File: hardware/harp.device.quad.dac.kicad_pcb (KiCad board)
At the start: 2 copper layers, 0 parts

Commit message: The footprint assigning and reviewing have started.
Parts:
- added C1: 100nF, Capacitor_SMD:C_0402_1005Metric, F.Cu at (122.2, 49.0)
- added C10: 10uF, Capacitor_SMD:C_0805_2012Metric, F.Cu at (118.5, 49.5)
- added C100: 100nF, Capacitor_SMD:C_0402_1005Metric, F.Cu at (77.7, 74.6)
- added C101: 100nF, Capacitor_SMD:C_0402_1005Metric, F.Cu at (77.7, 76.6)
- added C102: 100nF, Capacitor_SMD:C_0402_1005Metric, F.Cu at (80.5, 70.7)
- added C103: 100nF, Capacitor_SMD:C_0402_1005Metric, F.Cu at (80.5, 72.7)
- added C104: 100nF, Capacitor_SMD:C_0402_1005Metric, F.Cu at (80.5, 74.6)
- added C105: 100nF, Capacitor_SMD:C_0402_1005Metric, F.Cu at (80.5, 76.6)
- added C106: 10uF, Capacitor_SMD:C_0805_2012Metric, F.Cu at (96.7, 66.6)
- added C107: 100nF, Capacitor_SMD:C_0402_1005Metric, F.Cu at (83.4, 70.7)
- added C108: 1uF, Capacitor_SMD:C_0402_1005Metric, F.Cu at (83.4, 72.7)
- added C109: 10uF, Capacitor_SMD:C_0805_2012Metric, F.Cu at (96.7, 69.6)
- added C11: 10uF, Capacitor_SMD:C_0805_2012Metric, F.Cu at (118.5, 52.6)
- added C110: 100nF, Capacitor_SMD:C_0402_1005Metric, F.Cu at (83.4, 74.6)
- added C111: 1uF, Capacitor_SMD:C_0402_1005Metric, F.Cu at (83.4, 76.6)
- added C112: 10uF, Capacitor_SMD:C_0805_2012Metric, F.Cu at (96.7, 72.6)
- added C113: 100nF, Capacitor_SMD:C_0402_1005Metric, F.Cu at (96.2, 95.6)
- added C114: 100nF, Capacitor_SMD:C_0402_1005Metric, F.Cu at (96.2, 97.6)
- added C115: 100nF, Capacitor_SMD:C_0402_1005Metric, F.Cu at (96.2, 99.5)
- added C116: 100nF, Capacitor_SMD:C_0402_1005Metric, F.Cu at (96.2, 101.5)
- added C117: 100nF, Capacitor_SMD:C_0402_1005Metric, F.Cu at (96.2, 103.5)
- added C118: 1uF, Capacitor_SMD:C_0402_1005Metric, F.Cu at (96.2, 105.5)
- added C119: 10uF, Capacitor_SMD:C_0805_2012Metric, F.Cu at (88.3, 81.1)
- added C12: 100nF, Capacitor_SMD:C_0402_1005Metric, F.Cu at (125.0, 53.0)
- added C120: 10uF, Capacitor_SMD:C_0805_2012Metric, F.Cu at (88.3, 84.1)
- added C121: 100nF, Capacitor_SMD:C_0402_1005Metric, F.Cu at (96.2, 107.4)
- added C122: 4.7uF, Capacitor_SMD:C_0805_2012Metric, F.Cu at (88.3, 87.1)
- added C123: 1uF, Capacitor_SMD:C_0402_1005Metric, F.Cu at (99.1, 95.6)
- added C124: 1uF, Capacitor_SMD:C_0402_1005Metric, F.Cu at (99.1, 97.6)
- added C125: 10uF, Capacitor_SMD:C_0805_2012Metric, F.Cu at (88.3, 90.1)
- added C126: 10uF, Capacitor_SMD:C_0805_2012Metric, F.Cu at (88.3, 93.1)
- added C127: 10uF, Capacitor_SMD:C_0805_2012Metric, F.Cu at (92.8, 81.1)
- added C128: 10uF, Capacitor_SMD:C_0805_2012Metric, F.Cu at (92.8, 84.1)
- added C129: 150pF, Capacitor_SMD:C_0402_1005Metric, F.Cu at (99.1, 99.5)
- added C13: 100nF, Capacitor_SMD:C_0402_1005Metric, F.Cu at (125.0, 54.9)
- added C130: 100nF, Capacitor_SMD:C_0402_1005Metric, F.Cu at (99.1, 101.5)
- added C131: 330pF, Capacitor_SMD:C_0402_1005Metric, F.Cu at (99.1, 103.5)
- added C132: 10pF, Capacitor_SMD:C_0402_1005Metric, F.Cu at (99.1, 105.5)
- added C133: 33nF, Capacitor_SMD:C_0402_1005Metric, F.Cu at (99.1, 107.4)
- added C134: 1nF, Capacitor_SMD:C_0402_1005Metric, F.Cu at (102.0, 95.6)
- added C135: 100nF, Capacitor_SMD:C_0402_1005Metric, F.Cu at (102.0, 97.6)
- added C136: 100nF, Capacitor_SMD:C_0402_1005Metric, F.Cu at (102.0, 99.5)
- added C137: 1uF, Capacitor_SMD:C_0402_1005Metric, F.Cu at (102.0, 101.5)
- added C138: 1uF, Capacitor_SMD:C_0402_1005Metric, F.Cu at (102.0, 103.5)
- added C139: 10uF, Capacitor_SMD:C_0805_2012Metric, F.Cu at (92.8, 87.1)
- added C14: 100nF, Capacitor_SMD:C_0402_1005Metric, F.Cu at (125.0, 56.9)
- added C140: 10uF, Capacitor_SMD:C_0805_2012Metric, F.Cu at (92.8, 90.1)
- added C141: 10uF, Capacitor_SMD:C_0805_2012Metric, F.Cu at (92.8, 93.1)
- added C142: 10uF, Capacitor_SMD:C_0805_2012Metric, F.Cu at (97.2, 81.1)
- added C143: 10uF, Capacitor_SMD:C_0805_2012Metric, F.Cu at (97.2, 84.1)
- added C144: 10uF, Capacitor_SMD:C_0805_2012Metric, F.Cu at (97.2, 87.1)
- added C145: 4.7uF, Capacitor_SMD:C_0805_2012Metric, F.Cu at (97.2, 90.1)
- added C146: 100nF, Capacitor_SMD:C_0402_1005Metric, F.Cu at (102.0, 105.5)
- added C147: 100nF, Capacitor_SMD:C_0402_1005Metric, F.Cu at (102.0, 107.4)
- added C148: 100nF, Capacitor_SMD:C_0402_1005Metric, F.Cu at (139.8, 101.8)
- added C149: 100nF, Capacitor_SMD:C_0402_1005Metric, F.Cu at (139.8, 103.7)
- added C15: 100nF, Capacitor_SMD:C_0402_1005Metric, F.Cu at (125.0, 58.9)
- added C150: 100nF, Capacitor_SMD:C_0402_1005Metric, F.Cu at (139.8, 105.7)
- added C151: 100nF, Capacitor_SMD:C_0402_1005Metric, F.Cu at (139.8, 107.7)
- added C16: 4.7uF, Capacitor_SMD:C_0805_2012Metric, F.Cu at (118.5, 55.6)
- added C17: 4.7uF, Capacitor_SMD:C_0805_2012Metric, F.Cu at (118.5, 58.6)
- added C18: 10uF, Capacitor_SMD:C_0805_2012Metric, F.Cu at (118.5, 61.6)
- added C19: 100nF, Capacitor_SMD:C_0402_1005Metric, F.Cu at (125.0, 60.9)
- added C2: 100nF, Capacitor_SMD:C_0402_1005Metric, F.Cu at (122.2, 51.0)
- added C20: 100nF, Capacitor_SMD:C_0402_1005Metric, F.Cu at (127.9, 49.0)
- added C21: 100nF, Capacitor_SMD:C_0402_1005Metric, F.Cu at (127.9, 51.0)
- added C22: 100nF, Capacitor_SMD:C_0402_1005Metric, F.Cu at (127.9, 53.0)
- added C23: 100nF, Capacitor_SMD:C_0402_1005Metric, F.Cu at (127.9, 54.9)
- added C24: 100nF, Capacitor_SMD:C_0402_1005Metric, F.Cu at (127.9, 56.9)
- added C25: 100nF, Capacitor_SMD:C_0402_1005Metric, F.Cu at (127.9, 58.9)
- added C26: 100nF, Capacitor_SMD:C_0402_1005Metric, F.Cu at (127.9, 60.9)
- added C27: 100nF, Capacitor_SMD:C_0402_1005Metric, F.Cu at (130.8, 49.0)
- added C28: 100nF, Capacitor_SMD:C_0402_1005Metric, F.Cu at (130.8, 51.0)
- added C29: 100nF, Capacitor_SMD:C_0402_1005Metric, F.Cu at (130.8, 53.0)
- added C3: 1nF, Capacitor_SMD:C_0402_1005Metric, F.Cu at (122.2, 53.0)
- added C30: 100nF, Capacitor_SMD:C_0402_1005Metric, F.Cu at (144.4, 49.0)
- added C31: 1uF, Capacitor_SMD:C_0402_1005Metric, F.Cu at (144.4, 51.0)
- added C32: 100nF, Capacitor_SMD:C_0402_1005Metric, F.Cu at (144.4, 53.0)
- added C33: 100nF, Capacitor_SMD:C_0402_1005Metric, F.Cu at (144.4, 54.9)
- added C34: 100nF, Capacitor_SMD:C_0402_1005Metric, F.Cu at (144.4, 56.9)
- added C35: 100nF, Capacitor_SMD:C_0402_1005Metric, F.Cu at (144.4, 58.9)
- added C36: 10uF, Capacitor_SMD:C_0805_2012Metric, F.Cu at (149.6, 63.3)
- added C37: 100nF, Capacitor_SMD:C_0402_1005Metric, F.Cu at (144.4, 60.9)
- added C38: 1uF, Capacitor_SMD:C_0402_1005Metric, F.Cu at (147.2, 49.0)
- added C39: 100nF, Capacitor_SMD:C_0402_1005Metric, F.Cu at (147.2, 51.0)
- added C4: 100nF, Capacitor_SMD:C_0402_1005Metric, F.Cu at (122.2, 54.9)
- added C40: 100nF, Capacitor_SMD:C_0402_1005Metric, F.Cu at (147.2, 53.0)
- added C41: 100nF, Capacitor_SMD:C_0402_1005Metric, F.Cu at (147.2, 54.9)
- added C42: 100nF, Capacitor_SMD:C_0402_1005Metric, F.Cu at (147.2, 56.9)
- added C43: 1uF, Capacitor_SMD:C_0402_1005Metric, F.Cu at (147.2, 58.9)
- added C44: 100nF, Capacitor_SMD:C_0402_1005Metric, F.Cu at (147.2, 60.9)
- added C45: 100nF, Capacitor_SMD:C_0402_1005Metric, F.Cu at (150.1, 49.0)
- added C46: 100nF, Capacitor_SMD:C_0402_1005Metric, F.Cu at (150.1, 51.0)
- added C47: 100nF, Capacitor_SMD:C_0402_1005Metric, F.Cu at (150.1, 53.0)
- added C48: 1uF, Capacitor_SMD:C_0402_1005Metric, F.Cu at (150.1, 54.9)
- added C49: 100nF, Capacitor_SMD:C_0402_1005Metric, F.Cu at (150.1, 56.9)
- added C5: 100nF, Capacitor_SMD:C_0402_1005Metric, F.Cu at (122.2, 56.9)
- added C50: 15pF, Capacitor_SMD:C_0402_1005Metric, F.Cu at (150.1, 58.9)
- added C51: 15pF, Capacitor_SMD:C_0402_1005Metric, F.Cu at (150.1, 60.9)
- added C52: 15pF, Capacitor_SMD:C_0402_1005Metric, F.Cu at (153.0, 49.0)
- added C53: 15pF, Capacitor_SMD:C_0402_1005Metric, F.Cu at (153.0, 51.0)
- added C54: 15pF, Capacitor_SMD:C_0402_1005Metric, F.Cu at (153.0, 53.0)
- added C55: 15pF, Capacitor_SMD:C_0402_1005Metric, F.Cu at (153.0, 54.9)
- added C56: 15pF, Capacitor_SMD:C_0402_1005Metric, F.Cu at (153.0, 56.9)
- added C57: 15pF, Capacitor_SMD:C_0402_1005Metric, F.Cu at (153.0, 58.9)
- added C58: 10uF, Capacitor_SMD:C_0805_2012Metric, F.Cu at (149.6, 66.3)
- added C59: 10uF, Capacitor_SMD:C_0805_2012Metric, F.Cu at (149.6, 69.4)
- added C6: 10nF, Capacitor_SMD:C_0402_1005Metric, F.Cu at (122.2, 58.9)
- added C60: 15pF, Capacitor_SMD:C_0402_1005Metric, F.Cu at (121.9, 76.8)
- added C61: 15pF, Capacitor_SMD:C_0402_1005Metric, F.Cu at (121.9, 78.7)
- added C62: 15pF, Capacitor_SMD:C_0402_1005Metric, F.Cu at (121.9, 80.7)
- added C63: 15pF, Capacitor_SMD:C_0402_1005Metric, F.Cu at (121.9, 82.7)
- added C64: 100nF, Capacitor_SMD:C_0402_1005Metric, F.Cu at (121.9, 84.6)
- added C65: 100nF, Capacitor_SMD:C_0402_1005Metric, F.Cu at (121.9, 86.6)
- added C66: 100nF, Capacitor_SMD:C_0402_1005Metric, F.Cu at (121.9, 88.6)
- added C67: 100nF, Capacitor_SMD:C_0402_1005Metric, F.Cu at (121.9, 90.5)
- added C68: 100nF, Capacitor_SMD:C_0402_1005Metric, F.Cu at (124.8, 76.8)
- added C69: 100nF, Capacitor_SMD:C_0402_1005Metric, F.Cu at (124.8, 78.7)
- added C7: 1uF, Capacitor_SMD:C_0402_1005Metric, F.Cu at (122.2, 60.9)
- added C70: 100nF, Capacitor_SMD:C_0402_1005Metric, F.Cu at (124.8, 80.7)
- added C71: 100nF, Capacitor_SMD:C_0402_1005Metric, F.Cu at (124.8, 82.7)
- added C72: 100nF, Capacitor_SMD:C_0402_1005Metric, F.Cu at (124.8, 84.6)
- added C73: 100nF, Capacitor_SMD:C_0402_1005Metric, F.Cu at (124.8, 86.6)
- added C74: 100nF, Capacitor_SMD:C_0402_1005Metric, F.Cu at (124.8, 88.6)
- added C75: 100nF, Capacitor_SMD:C_0402_1005Metric, F.Cu at (124.8, 90.5)
- added C76: 100nF, Capacitor_SMD:C_0402_1005Metric, F.Cu at (127.7, 76.8)
- added C77: 100nF, Capacitor_SMD:C_0402_1005Metric, F.Cu at (127.7, 78.7)
- added C78: 100nF, Capacitor_SMD:C_0402_1005Metric, F.Cu at (127.7, 80.7)
- added C79: 100nF, Capacitor_SMD:C_0402_1005Metric, F.Cu at (127.7, 82.7)
- added C8: 1uF, Capacitor_SMD:C_0402_1005Metric, F.Cu at (125.0, 49.0)
- added C80: 15pF, Capacitor_SMD:C_0402_1005Metric, F.Cu at (127.7, 84.6)
- added C81: 15pF, Capacitor_SMD:C_0402_1005Metric, F.Cu at (127.7, 86.6)
- added C82: 15pF, Capacitor_SMD:C_0402_1005Metric, F.Cu at (127.7, 88.6)
- added C83: 15pF, Capacitor_SMD:C_0402_1005Metric, F.Cu at (127.7, 90.5)
- added C84: 100nF, Capacitor_SMD:C_0402_1005Metric, F.Cu at (130.5, 76.8)
- added C85: 100nF, Capacitor_SMD:C_0402_1005Metric, F.Cu at (130.5, 78.7)
- added C86: 100nF, Capacitor_SMD:C_0402_1005Metric, F.Cu at (130.5, 80.7)
- added C87: 100nF, Capacitor_SMD:C_0402_1005Metric, F.Cu at (130.5, 82.7)
- added C88: 100nF, Capacitor_SMD:C_0402_1005Metric, F.Cu at (130.5, 84.6)
- added C89: 100nF, Capacitor_SMD:C_0402_1005Metric, F.Cu at (130.5, 86.6)
- added C9: 100nF, Capacitor_SMD:C_0402_1005Metric, F.Cu at (125.0, 51.0)
- added C90: 100nF, Capacitor_SMD:C_0402_1005Metric, F.Cu at (130.5, 88.6)
- added C91: 100nF, Capacitor_SMD:C_0402_1005Metric, F.Cu at (130.5, 90.5)
- added C92: 100nF, Capacitor_SMD:C_0402_1005Metric, F.Cu at (148.3, 76.8)
- added C93: 100nF, Capacitor_SMD:C_0402_1005Metric, F.Cu at (148.3, 78.7)
- added C94: 100nF, Capacitor_SMD:C_0402_1005Metric, F.Cu at (148.3, 80.7)
- added C95: 1uF, Capacitor_SMD:C_0402_1005Metric, F.Cu at (148.3, 82.7)
- added C96: 1uF, Capacitor_SMD:C_0402_1005Metric, F.Cu at (148.3, 84.6)
- added C97: 100nF, Capacitor_SMD:C_0402_1005Metric, F.Cu at (148.3, 86.6)
- added C98: 1uF, Capacitor_SMD:C_0402_1005Metric, F.Cu at (77.7, 70.7)
- added C99: 100nF, Capacitor_SMD:C_0402_1005Metric, F.Cu at (77.7, 72.7)
- added D1: BAT43W-V, Diode_SMD:D_SOD-123, F.Cu at (123.4, 93.2)
- added D2: BAT43W-V, Diode_SMD:D_SOD-123, F.Cu at (123.4, 96.6)
- added D3: BAT43W-V, Diode_SMD:D_SOD-123, F.Cu at (123.4, 99.9)
- added D4: BAT43W-V, Diode_SMD:D_SOD-123, F.Cu at (123.4, 103.3)
- added D7: BZV55B15, Diode_SMD:D_MiniMELF, F.Cu at (79.4, 97.9)
- added D8: BZV55B15, Diode_SMD:D_MiniMELF, F.Cu at (79.4, 101.2)
- added FID1: Fiducial, Fiducial:Fiducial_0.5mm_Mask1mm, F.Cu at (130.7, 63.1)
- added FID2: Fiducial, Fiducial:Fiducial_0.5mm_Mask1mm, F.Cu at (130.7, 65.7)
- added FID3: Fiducial, Fiducial:Fiducial_0.5mm_Mask1mm, F.Cu at (130.7, 68.2)
- added FID4: Fiducial, Fiducial:Fiducial_0.5mm_Mask1mm, F.Cu at (130.7, 70.8)
- added J2: Conn_01x03_Male, Connector_PinHeader_2.54mm:PinHeader_1x03_P2.54mm_Vertical, F.Cu at (152.1, 78.1)
- added J3: USB_C_Receptacle_USB2.0, Connector_USB:USB_C_Receptacle_JAE_DX07S016JA1R1500, F.Cu at (140.0, 92.6)
- added J4: AudioJack3, Connector_Audio:Jack_3.5mm_CUI_SJ-3524-SMT_Horizontal, F.Cu at (82.3, 57.6)
- added J9: Barrel_Jack_Switch, Connector_BarrelJack:BarrelJack_CUI_PJ-102AH_Horizontal, F.Cu at (94.0, 50.4)
- added LED1: LED, LED_SMD:LED_0603_1608Metric_Pad1.05x0.95mm_HandSolder, F.Cu at (118.5, 64.4)
- added LED2: LED, LED_SMD:LED_0603_1608Metric_Pad1.05x0.95mm_HandSolder, F.Cu at (118.5, 67.0)
- added LED3: LED, LED_SMD:LED_0603_1608Metric_Pad1.05x0.95mm_HandSolder, F.Cu at (118.5, 69.6)
- added LED4: LED, LED_SMD:LED_0603_1608Metric_Pad1.05x0.95mm_HandSolder, F.Cu at (145.2, 63.1)
- added LED5: LED, LED_SMD:LED_0603_1608Metric_Pad1.05x0.95mm_HandSolder, F.Cu at (145.2, 65.7)
- added LED6: LED, LED_SMD:LED_0603_1608Metric_Pad1.05x0.95mm_HandSolder, F.Cu at (145.2, 68.3)
- added LED7: LED, LED_SMD:LED_0603_1608Metric_Pad1.05x0.95mm_HandSolder, F.Cu at (145.2, 70.9)
- added LED8: LED, LED_SMD:LED_0603_1608Metric_Pad1.05x0.95mm_HandSolder, F.Cu at (155.1, 95.0)
- added LED9: LED, LED_SMD:LED_0603_1608Metric_Pad1.05x0.95mm_HandSolder, F.Cu at (78.4, 104.2)
- added R1: 100, Resistor_SMD:R_0402_1005Metric, F.Cu at (122.2, 62.8)
- added R10: 201, Resistor_SMD:R_0402_1005Metric, F.Cu at (125.1, 68.8)
- added R100: 1.10k, Resistor_SMD:R_0402_1005Metric, F.Cu at (87.5, 97.6)
- added R101: 4.27k, Resistor_SMD:R_0402_1005Metric, F.Cu at (87.5, 99.6)
- added R102: 1.42k, Resistor_SMD:R_0402_1005Metric, F.Cu at (87.5, 101.6)
- added R103: 1.82k, Resistor_SMD:R_0402_1005Metric, F.Cu at (87.5, 103.6)
- added R104: 2.74k, Resistor_SMD:R_0402_1005Metric, F.Cu at (87.5, 105.6)
- added R105: 1.18k, Resistor_SMD:R_0402_1005Metric, F.Cu at (87.5, 107.6)
- added R106: 11.8k, Resistor_SMD:R_0402_1005Metric, F.Cu at (90.4, 95.6)
- added R107: 470, Resistor_SMD:R_0402_1005Metric, F.Cu at (90.4, 97.6)
- added R108: 57.6k, Resistor_SMD:R_0402_1005Metric, F.Cu at (90.4, 99.6)
- added R109: 365k, Resistor_SMD:R_0402_1005Metric, F.Cu at (90.4, 101.6)
- added R11: 201, Resistor_SMD:R_0402_1005Metric, F.Cu at (125.1, 70.8)
- added R110: 1.5k, Resistor_SMD:R_0402_1005Metric, F.Cu at (90.4, 103.6)
- added R111: 130k, Resistor_SMD:R_0402_1005Metric, F.Cu at (90.4, 105.6)
- added R112: 11.3k, Resistor_SMD:R_0402_1005Metric, F.Cu at (90.4, 107.6)
- added R113: 100k, Resistor_SMD:R_0402_1005Metric, F.Cu at (93.3, 95.6)
- added R114: 24.9k, Resistor_SMD:R_0402_1005Metric, F.Cu at (93.3, 97.6)
- added R115: 100k, Resistor_SMD:R_0402_1005Metric, F.Cu at (93.3, 99.6)
- added R116: 13.7k, Resistor_SMD:R_0402_1005Metric, F.Cu at (93.3, 101.6)
- added R117: 80.6k, Resistor_SMD:R_0402_1005Metric, F.Cu at (93.3, 103.6)
- added R118: 0, Resistor_SMD:R_0402_1005Metric, F.Cu at (93.3, 105.6)
- added R119: 0, Resistor_SMD:R_0402_1005Metric, F.Cu at (93.3, 107.6)
- added R12: 330, Resistor_SMD:R_0402_1005Metric, F.Cu at (125.1, 72.8)
- added R120: 10, Resistor_SMD:R_0603_1608Metric_Pad0.98x0.95mm_HandSolder, F.Cu at (136.1, 102.0)
- added R121: 10, Resistor_SMD:R_0603_1608Metric_Pad0.98x0.95mm_HandSolder, F.Cu at (136.1, 104.5)
- added R122: 10, Resistor_SMD:R_0603_1608Metric_Pad0.98x0.95mm_HandSolder, F.Cu at (136.1, 107.1)
- added R123: 10, Resistor_SMD:R_0603_1608Metric_Pad0.98x0.95mm_HandSolder, F.Cu at (136.1, 109.6)
- added R13: 330, Resistor_SMD:R_0402_1005Metric, F.Cu at (128.0, 62.8)
- added R14: 330, Resistor_SMD:R_0402_1005Metric, F.Cu at (128.0, 64.8)
- added R15: 10K, Resistor_SMD:R_0402_1005Metric, F.Cu at (128.0, 66.8)
- added R16: 10K, Resistor_SMD:R_0402_1005Metric, F.Cu at (128.0, 68.8)
- added R17: 10K, Resistor_SMD:R_0402_1005Metric, F.Cu at (128.0, 70.8)
- added R18: 330, Resistor_SMD:R_0402_1005Metric, F.Cu at (135.7, 49.0)
- added R19: 330, Resistor_SMD:R_0402_1005Metric, F.Cu at (135.7, 51.0)
- added R2: 1K, Resistor_SMD:R_0402_1005Metric, F.Cu at (122.2, 64.8)
- added R20: 330, Resistor_SMD:R_0402_1005Metric, F.Cu at (135.7, 53.0)
- added R21: 330, Resistor_SMD:R_0402_1005Metric, F.Cu at (135.7, 55.0)
- added R22: 100, Resistor_SMD:R_0402_1005Metric, F.Cu at (135.7, 57.0)
- added R23: 40.2k, Resistor_SMD:R_0402_1005Metric, F.Cu at (135.7, 59.0)
- added R24: 40.2k, Resistor_SMD:R_0402_1005Metric, F.Cu at (135.7, 61.0)
- added R25: 40.2k, Resistor_SMD:R_0402_1005Metric, F.Cu at (138.6, 49.0)
- added R26: 40.2k, Resistor_SMD:R_0402_1005Metric, F.Cu at (138.6, 51.0)
- added R27: 40.2k, Resistor_SMD:R_0402_1005Metric, F.Cu at (138.6, 53.0)
- added R28: 40.2k, Resistor_SMD:R_0402_1005Metric, F.Cu at (138.6, 55.0)
- added R29: 40.2k, Resistor_SMD:R_0402_1005Metric, F.Cu at (138.6, 57.0)
- added R3: 10, Resistor_SMD:R_0402_1005Metric, F.Cu at (122.2, 66.8)
- added R30: 40.2k, Resistor_SMD:R_0402_1005Metric, F.Cu at (138.6, 59.0)
- added R31: 10k, Resistor_SMD:R_0402_1005Metric, F.Cu at (138.6, 61.0)
- added R32: 10k, Resistor_SMD:R_0402_1005Metric, F.Cu at (141.5, 49.0)
- added R33: 10k, Resistor_SMD:R_0402_1005Metric, F.Cu at (141.5, 51.0)
- added R34: 10k, Resistor_SMD:R_0402_1005Metric, F.Cu at (141.5, 53.0)
- added R35: 10k, Resistor_SMD:R_0402_1005Metric, F.Cu at (141.5, 55.0)
- added R36: 10k, Resistor_SMD:R_0402_1005Metric, F.Cu at (141.5, 57.0)
- added R37: 10k, Resistor_SMD:R_0402_1005Metric, F.Cu at (141.5, 59.0)
- added R38: 10k, Resistor_SMD:R_0402_1005Metric, F.Cu at (141.5, 61.0)
- added R39: 4.02k, Resistor_SMD:R_0402_1005Metric, F.Cu at (107.4, 76.8)
- added R4: 10, Resistor_SMD:R_0402_1005Metric, F.Cu at (122.2, 68.8)
- added R40: 4.02k, Resistor_SMD:R_0402_1005Metric, F.Cu at (107.4, 78.8)
- added R41: 4.02k, Resistor_SMD:R_0402_1005Metric, F.Cu at (107.4, 80.8)
- added R42: 4.02k, Resistor_SMD:R_0402_1005Metric, F.Cu at (107.4, 82.7)
- added R43: 40.2k, Resistor_SMD:R_0402_1005Metric, F.Cu at (107.4, 84.7)
- added R44: 40.2k, Resistor_SMD:R_0402_1005Metric, F.Cu at (107.4, 86.7)
- added R45: 40.2k, Resistor_SMD:R_0402_1005Metric, F.Cu at (107.4, 88.7)
- added R46: 40.2k, Resistor_SMD:R_0402_1005Metric, F.Cu at (107.4, 90.7)
- added R47: 100k, Resistor_SMD:R_0402_1005Metric, F.Cu at (107.4, 92.7)
- added R48: 100k, Resistor_SMD:R_0402_1005Metric, F.Cu at (110.3, 76.8)
- added R49: 100k, Resistor_SMD:R_0402_1005Metric, F.Cu at (110.3, 78.8)
- added R5: 10, Resistor_SMD:R_0402_1005Metric, F.Cu at (122.2, 70.8)
- added R50: 100k, Resistor_SMD:R_0402_1005Metric, F.Cu at (110.3, 80.8)
- added R51: 4.75k, Resistor_SMD:R_0402_1005Metric, F.Cu at (110.3, 82.7)
- added R52: 4.75k, Resistor_SMD:R_0402_1005Metric, F.Cu at (110.3, 84.7)
- added R53: 4.75k, Resistor_SMD:R_0402_1005Metric, F.Cu at (110.3, 86.7)
- added R54: 4.75k, Resistor_SMD:R_0402_1005Metric, F.Cu at (110.3, 88.7)
- added R55: 4.75k, Resistor_SMD:R_0402_1005Metric, F.Cu at (110.3, 90.7)
- added R56: 4.75k, Resistor_SMD:R_0402_1005Metric, F.Cu at (110.3, 92.7)
- added R57: 4.75k, Resistor_SMD:R_0402_1005Metric, F.Cu at (113.2, 76.8)
- added R58: 4.75k, Resistor_SMD:R_0402_1005Metric, F.Cu at (113.2, 78.8)
- added R59: 47.5k, Resistor_SMD:R_0402_1005Metric, F.Cu at (113.2, 80.8)
- added R6: 10K, Resistor_SMD:R_0402_1005Metric, F.Cu at (122.2, 72.8)
- added R60: 10k, Resistor_SMD:R_0402_1005Metric, F.Cu at (113.2, 82.7)
- added R61: 47.5k, Resistor_SMD:R_0402_1005Metric, F.Cu at (113.2, 84.7)
- added R62: 10k, Resistor_SMD:R_0402_1005Metric, F.Cu at (113.2, 86.7)
- added R63: 47.5k, Resistor_SMD:R_0402_1005Metric, F.Cu at (113.2, 88.7)
- added R64: 10k, Resistor_SMD:R_0402_1005Metric, F.Cu at (113.2, 90.7)
- added R65: 47.5k, Resistor_SMD:R_0402_1005Metric, F.Cu at (113.2, 92.7)
- added R66: 10k, Resistor_SMD:R_0402_1005Metric, F.Cu at (116.1, 76.8)
- added R67: 40.2k, Resistor_SMD:R_0402_1005Metric, F.Cu at (116.1, 78.8)
- added R68: 40.2k, Resistor_SMD:R_0402_1005Metric, F.Cu at (116.1, 80.8)
- added R69: 40.2k, Resistor_SMD:R_0402_1005Metric, F.Cu at (116.1, 82.7)
- added R7: 10K, Resistor_SMD:R_0402_1005Metric, F.Cu at (125.1, 62.8)
- added R70: 40.2k, Resistor_SMD:R_0402_1005Metric, F.Cu at (116.1, 84.7)
- added R71: 10, Resistor_SMD:R_0402_1005Metric, F.Cu at (116.1, 86.7)
- added R72: 10, Resistor_SMD:R_0402_1005Metric, F.Cu at (116.1, 88.7)
- added R73: 10, Resistor_SMD:R_0402_1005Metric, F.Cu at (116.1, 90.7)
- added R74: 10, Resistor_SMD:R_0402_1005Metric, F.Cu at (116.1, 92.7)
- added R75: 4.02k, Resistor_SMD:R_0402_1005Metric, F.Cu at (119.0, 76.8)
- added R76: 4.02k, Resistor_SMD:R_0402_1005Metric, F.Cu at (119.0, 78.8)
- added R77: 4.02k, Resistor_SMD:R_0402_1005Metric, F.Cu at (119.0, 80.8)
- added R78: 4.02k, Resistor_SMD:R_0402_1005Metric, F.Cu at (119.0, 82.7)
- added R79: 10k, Resistor_SMD:R_0402_1005Metric, F.Cu at (119.0, 84.7)
- added R8: 10K, Resistor_SMD:R_0402_1005Metric, F.Cu at (125.1, 64.8)
- added R80: 10k, Resistor_SMD:R_0402_1005Metric, F.Cu at (119.0, 86.7)
- added R81: 10k, Resistor_SMD:R_0402_1005Metric, F.Cu at (119.0, 88.7)
- added R82: 10k, Resistor_SMD:R_0402_1005Metric, F.Cu at (119.0, 90.7)
- added R83: 0, Resistor_SMD:R_0402_1005Metric, F.Cu at (147.4, 88.7)
- added R84: 100k, Resistor_SMD:R_0402_1005Metric, F.Cu at (147.4, 90.7)
- added R85: 470, Resistor_SMD:R_0402_1005Metric, F.Cu at (147.4, 92.7)
- added R86: 5.1k, Resistor_SMD:R_0402_1005Metric, F.Cu at (150.3, 88.7)
- added R87: 5.1k, Resistor_SMD:R_0402_1005Metric, F.Cu at (150.3, 90.7)
- added R88: 24, Resistor_SMD:R_0402_1005Metric, F.Cu at (150.3, 92.7)
- added R89: 24, Resistor_SMD:R_0402_1005Metric, F.Cu at (153.2, 88.7)
- added R9: 27, Resistor_SMD:R_0402_1005Metric, F.Cu at (125.1, 66.8)
- added R90: 24, Resistor_SMD:R_0402_1005Metric, F.Cu at (153.2, 90.7)
- added R91: 24, Resistor_SMD:R_0402_1005Metric, F.Cu at (153.2, 92.7)
- added R92: 100, Resistor_SMD:R_0402_1005Metric, F.Cu at (102.5, 49.0)
- added R93: 100, Resistor_SMD:R_0402_1005Metric, F.Cu at (102.5, 51.0)
- added R94: 100, Resistor_SMD:R_0402_1005Metric, F.Cu at (102.5, 53.0)
- added R95: 100, Resistor_SMD:R_0402_1005Metric, F.Cu at (102.5, 55.0)
- added R96: 100, Resistor_SMD:R_0402_1005Metric, F.Cu at (102.5, 57.0)
- added R97: 5.1k, Resistor_SMD:R_0402_1005Metric, F.Cu at (102.5, 59.0)
- added R98: 5.1k, Resistor_SMD:R_0402_1005Metric, F.Cu at (102.5, 61.0)
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
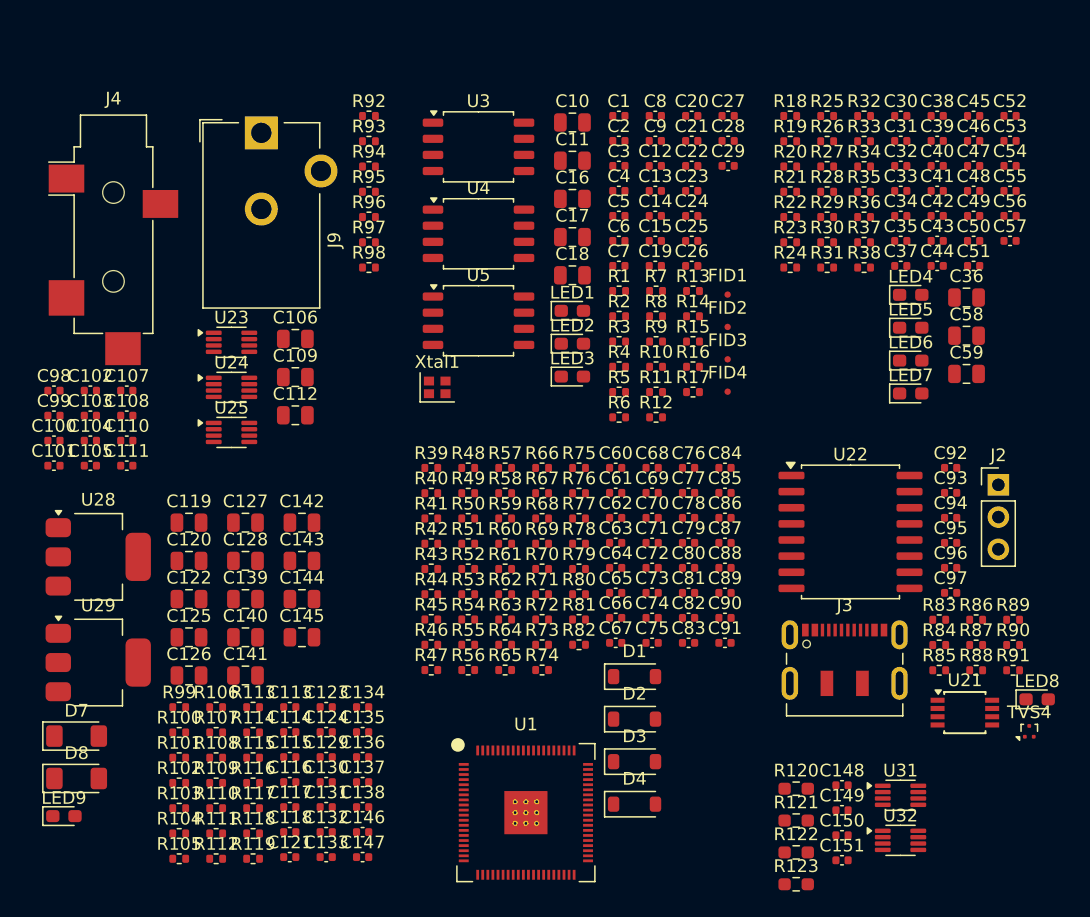
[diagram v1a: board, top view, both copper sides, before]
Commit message: Updating some footprints
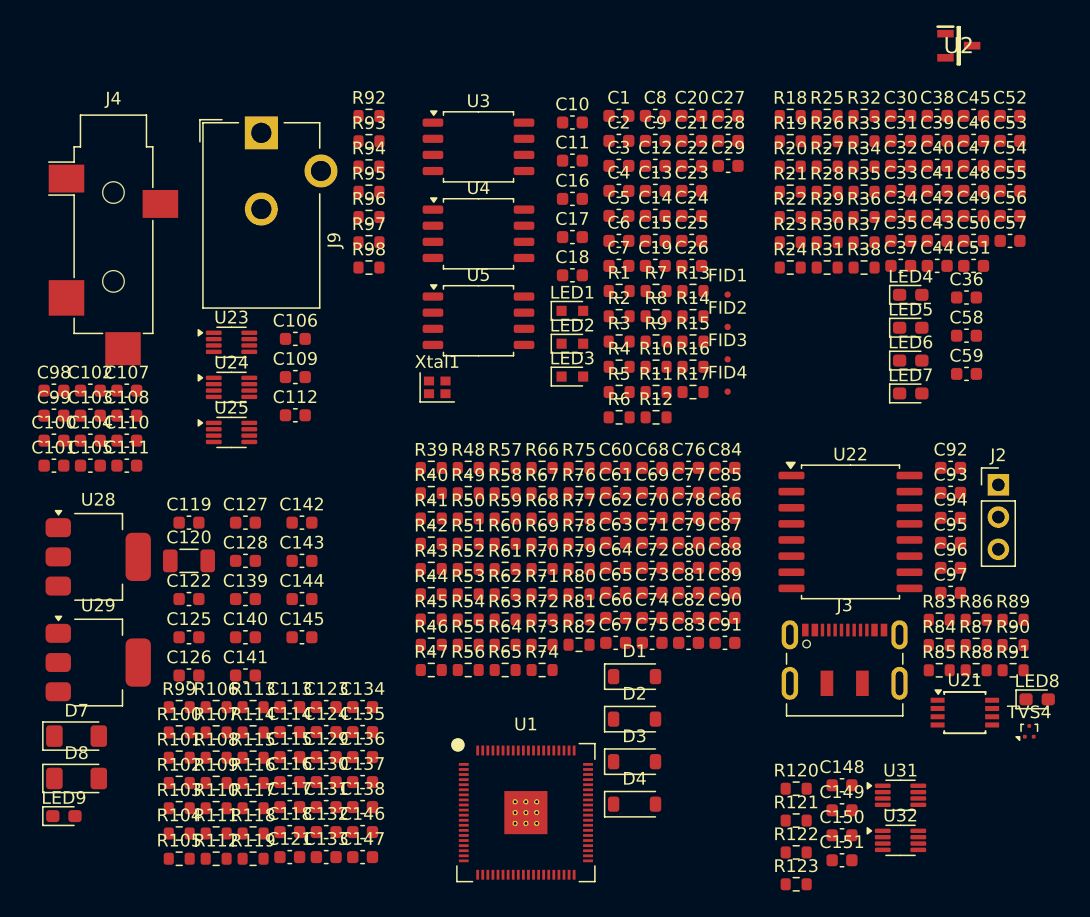
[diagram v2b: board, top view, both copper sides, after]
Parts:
- added U2: LM4040A30IDBZR, harp.device.quad.dac.kicad:SOT95P237X112-3N, F.Cu at (148.9, 43.5)
- C1, C100, C101, C102, C103, C104, C105, C107, C108, C110, C111, C113, C114, C115, C116, C117, C118, C12, C121, C123, C124, C129, C13, C130, C131, C132, C133, C134, C135, C136, C137, C138, C14, C146, C147, C148, C149, C15, C150, C151, C19, C2, C20, C21, C22, C23, C24, C25, C26, C27, C28, C29, C3, C30, C31, C32, C33, C34, C35, C37, C38, C39, C4, C40, C41, C42, C43, C44, C45, C46, C47, C48, C49, C5, C50, C51, C52, C53, C54, C55, C56, C57, C6, C60, C61, C62, C63, C64, C65, C66, C67, C68, C69, C7, C70, C71, C72, C73, C74, C75, C76, C77, C78, C79, C8, C80, C81, C82, C83, C84, C85, C86, C87, C88, C89, C9, C90, C91, C92, C93, C94, C95, C96, C97, C98, C99: footprint Capacitor_SMD:C_0402_1005Metric -> Capacitor_SMD:C_0603_1608Metric
- C10, C106, C109, C11, C112, C119, C122, C125, C126, C127, C128, C139, C140, C141, C142, C143, C144, C145, C16, C17, C18, C36, C58, C59: footprint Capacitor_SMD:C_0805_2012Metric -> Capacitor_SMD:C_0603_1608Metric
- C120: footprint Capacitor_SMD:C_0805_2012Metric -> Capacitor_SMD:C_1206_3216Metric
- LED1, LED2, LED3: footprint LED_SMD:LED_0603_1608Metric_Pad1.05x0.95mm_HandSolder -> harp.device.quad.dac.kicad:LED_0603_1608Metric_Pad1.05x0.95mm_HandSolder
- R1, R10, R100, R101, R102, R103, R104, R105, R106, R107, R108, R109, R11, R110, R111, R112, R113, R114, R115, R116, R117, R118, R119, R12, R13, R14, R15, R16, R17, R18, R19, R2, R20, R21, R22, R23, R24, R25, R26, R27, R28, R29, R3, R30, R31, R32, R33, R34, R35, R36, R37, R38, R39, R4, R40, R41, R42, R43, R44, R45, R46, R47, R48, R49, R5, R50, R51, R52, R53, R54, R55, R56, R57, R58, R59, R6, R60, R61, R62, R63, R64, R65, R66, R67, R68, R69, R7, R70, R71, R72, R73, R74, R75, R76, R77, R78, R79, R8, R80, R81, R82, R83, R84, R85, R86, R87, R88, R89, R9, R90, R91, R92, R93, R94, R95, R96, R97, R98, R99: footprint Resistor_SMD:R_0402_1005Metric -> Resistor_SMD:R_0603_1608Metric
- R120, R121, R122, R123: footprint Resistor_SMD:R_0603_1608Metric_Pad0.98x0.95mm_HandSolder -> Resistor_SMD:R_0603_1608Metric
- U3, U4, U5: footprint Package_SO:SOIC-8_5.3x5.3mm_P1.27mm -> harp.device.quad.dac.kicad:SOIC-8_5.3x5.3mm_P1.27mm

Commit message: The layout design has begun.
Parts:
- added CMC1: L_Coupled_1423, harp.device.quad.dac.kicad:L_CommonModeChoke_TDKCorporation_1210, F.Cu at (404.0, 23.0)
- added D5: V40D103C-M3_I, harp.device.quad.dac.kicad:V40D103CM3I, F.Cu at (399.0, 34.0)
- added D6: CBAT54S_TR_PBFREE, harp.device.quad.dac.kicad:SOT95P230X109-3N, F.Cu at (412.0, 249.7)
- added J1: Conn_01x04_Pin, Connector_PinHeader_2.54mm:PinHeader_1x04_P2.54mm_Vertical, F.Cu at (103.0, -40.8)
- added J11: Conn_Coaxial, harp.device.quad.dac.kicad:SMA_TE_Connectivity_CONSMA002-SMD-G-T_Horizontal, F.Cu at (222.8, -107.6)
- added J12: Conn_Coaxial, harp.device.quad.dac.kicad:SMA_TE_Connectivity_CONSMA002-SMD-G-T_Horizontal, F.Cu at (222.8, -98.4)
- added J13: Conn_Coaxial, harp.device.quad.dac.kicad:SMA_TE_Connectivity_CONSMA002-SMD-G-T_Horizontal, F.Cu at (194.0, -108.0)
- added J14: Conn_Coaxial, harp.device.quad.dac.kicad:SMA_TE_Connectivity_CONSMA002-SMD-G-T_Horizontal, F.Cu at (194.0, -98.8)
- added J15: Conn_Coaxial, harp.device.quad.dac.kicad:SMA_TE_Connectivity_CONSMA002-SMD-G-T_Horizontal, F.Cu at (303.0, -77.2)
- added J16: Conn_Coaxial, harp.device.quad.dac.kicad:SMA_TE_Connectivity_CONSMA002-SMD-G-T_Horizontal, F.Cu at (303.0, -68.0)
- added J17: Conn_Coaxial, harp.device.quad.dac.kicad:SMA_TE_Connectivity_CONSMA002-SMD-G-T_Horizontal, F.Cu at (312.2, -77.2)
- added J18: Conn_Coaxial, harp.device.quad.dac.kicad:SMA_TE_Connectivity_CONSMA002-SMD-G-T_Horizontal, F.Cu at (312.2, -68.0)
- added J19: Conn_01x02, Connector_PinHeader_2.54mm:PinHeader_1x02_P2.54mm_Vertical, F.Cu at (-322.5, -203.6)
- added J20: Conn_01x02, Connector_PinHeader_2.54mm:PinHeader_1x02_P2.54mm_Vertical, F.Cu at (-377.8, 81.3)
- added J21: Conn_01x02, Connector_PinHeader_2.54mm:PinHeader_1x02_P2.54mm_Vertical, F.Cu at (-373.2, 81.3)
- added J22: Conn_01x02, Connector_PinHeader_2.54mm:PinHeader_1x02_P2.54mm_Vertical, F.Cu at (86.3, -105.0)
- added J23: Conn_01x02, Connector_PinHeader_2.54mm:PinHeader_1x02_P2.54mm_Vertical, F.Cu at (91.0, -105.0)
- added J24: Conn_01x02, Connector_PinHeader_2.54mm:PinHeader_1x02_P2.54mm_Vertical, F.Cu at (193.0, -17.0)
- added J25: Conn_01x02, Connector_PinHeader_2.54mm:PinHeader_1x02_P2.54mm_Vertical, F.Cu at (439.0, 231.7)
- added J26: Conn_01x02, Connector_PinHeader_2.54mm:PinHeader_1x02_P2.54mm_Vertical, F.Cu at (409.0, 171.0)
- added J27: USB_C_Receptacle_USB2.0, harp.device.quad.dac.kicad:USB_C_Receptacle_JAE_DX07S016JA1R1500, F.Cu at (424.0, 35.0)
- added J5: Conn_Coaxial, harp.device.quad.dac.kicad:SMA_TE_Connectivity_CONSMA002-SMD-G-T_Horizontal, F.Cu at (254.0, 63.5)
- added J6: Conn_Coaxial, harp.device.quad.dac.kicad:SMA_TE_Connectivity_CONSMA002-SMD-G-T_Horizontal, F.Cu at (254.0, 50.8)
- added J7: Conn_Coaxial, harp.device.quad.dac.kicad:SMA_TE_Connectivity_CONSMA002-SMD-G-T_Horizontal, F.Cu at (254.0, 88.9)
- added J8: Conn_Coaxial, harp.device.quad.dac.kicad:SMA_TE_Connectivity_CONSMA002-SMD-G-T_Horizontal, F.Cu at (254.0, 76.2)
- added Jump1: SolderJumper_2_Open, harp.device.quad.dac.kicad:R_0603_1608Metric_Pad0.98x0.95mm_HandSolder, F.Cu at (-318.0, -200.0)
- added Jump2: SolderJumper_2_Open, harp.device.quad.dac.kicad:R_0603_1608Metric_Pad0.98x0.95mm_HandSolder, F.Cu at (-378.0, 87.5)
- added Jump3: SolderJumper_2_Open, harp.device.quad.dac.kicad:R_0603_1608Metric_Pad0.98x0.95mm_HandSolder, F.Cu at (-378.0, 90.0)
- added Jump4: SolderJumper_2_Open, harp.device.quad.dac.kicad:R_0603_1608Metric_Pad0.98x0.95mm_HandSolder, F.Cu at (86.2, -98.9)
- added Jump5: SolderJumper_2_Open, harp.device.quad.dac.kicad:R_0603_1608Metric_Pad0.98x0.95mm_HandSolder, F.Cu at (86.2, -96.4)
- added Jump6: SolderJumper_2_Open, harp.device.quad.dac.kicad:R_0603_1608Metric_Pad0.98x0.95mm_HandSolder, F.Cu at (204.0, -13.0)
- added Jump7: SolderJumper_2_Open, harp.device.quad.dac.kicad:R_0603_1608Metric_Pad0.98x0.95mm_HandSolder, F.Cu at (434.0, 253.7)
- added Jump8: SolderJumper_2_Open, harp.device.quad.dac.kicad:R_0603_1608Metric_Pad0.98x0.95mm_HandSolder, F.Cu at (404.2, 179.6)
- added L1: XGL3530-332MEC, harp.device.quad.dac.kicad:XGL3530332MEC, F.Cu at (-308.0, -183.0)
- added L2: XAL6030-332MEC, harp.device.quad.dac.kicad:XAL6030182MEB, F.Cu at (407.0, 241.7)
- added L3: 744778910, harp.device.quad.dac.kicad:WE-PD_7332-7345_PLASTIC_BASE54, F.Cu at (411.0, 180.0)
- added REF**: MountingHole_3.2mm_M3_DIN965, harp.device.quad.dac.kicad:MountingHole_3.2mm_M3_DIN965, F.Cu at (154.0, 43.0)
- added REF**: MountingHole_3.2mm_M3_DIN965, harp.device.quad.dac.kicad:MountingHole_3.2mm_M3_DIN965, F.Cu at (154.0, 87.0)
- added REF**: MountingHole_3.2mm_M3_DIN965, harp.device.quad.dac.kicad:MountingHole_3.2mm_M3_DIN965, F.Cu at (256.0, 96.5)
- added REF**: MountingHole_3.2mm_M3_DIN965, harp.device.quad.dac.kicad:MountingHole_3.2mm_M3_DIN965, F.Cu at (256.0, 43.0)
- added RShunt1: CRCW120610R0FKEBC, Resistor_SMD:R_1206_3216Metric, F.Cu at (-335.0, 64.0)
- added RShunt2: CRCW120610R0FKEBC, Resistor_SMD:R_1206_3216Metric, F.Cu at (-336.0, 90.0)
- added RShunt3: CRCW120610R0FKEBC, Resistor_SMD:R_1206_3216Metric, F.Cu at (-335.5, 112.6)
- added RShunt4: CRCW120610R0FKEBC, Resistor_SMD:R_1206_3216Metric, F.Cu at (-352.0, 141.0)
- added SW1: ~, harp.device.quad.dac.kicad:SW_Push_1P1T-SH_NO_Vertical_Wuerth_WS-TASV, F.Cu at (-352.0, -202.0)
- added SW2: ~, harp.device.quad.dac.kicad:SW_Push_1P1T-SH_NO_Vertical_Wuerth_WS-TASV, F.Cu at (-352.0, -191.0)
- added SW3: ~, harp.device.quad.dac.kicad:SW_Push_1P1T-SH_NO_Vertical_Wuerth_WS-TASV, F.Cu at (-352.0, -182.0)
- added SW4: ~, harp.device.quad.dac.kicad:SW_Push_1P1T-SH_NO_Vertical_Wuerth_WS-TASV, F.Cu at (-352.0, -170.0)
- added SW5: ~, harp.device.quad.dac.kicad:SW_Push_1P1T-SH_NO_Vertical_Wuerth_WS-TASV, F.Cu at (-352.0, -162.0)
- added TVS1: ESD441DPLR, harp.device.quad.dac.kicad:ESD441DPLR, F.Cu at (89.8, -99.4)
- added TVS10: ESD441DPLR, harp.device.quad.dac.kicad:ESD441DPLR, F.Cu at (199.0, -14.0)
- added TVS11: ESD441DPLR, harp.device.quad.dac.kicad:ESD441DPLR, F.Cu at (412.0, 34.0)
- added TVS12: ESD441DPLR, harp.device.quad.dac.kicad:ESD441DPLR, F.Cu at (232.0, -108.5)
- added TVS13: ESD441DPLR, harp.device.quad.dac.kicad:ESD441DPLR, F.Cu at (232.0, -107.0)
- added TVS14: ESD441DPLR, harp.device.quad.dac.kicad:ESD441DPLR, F.Cu at (202.0, -111.5)
- added TVS15: ESD441DPLR, harp.device.quad.dac.kicad:ESD441DPLR, F.Cu at (202.0, -110.0)
- added TVS2: CDDFN10-3324P, harp.device.quad.dac.kicad:CDDFN103324P, F.Cu at (108.0, -36.0)
- added TVS3: ESD441DPLR, harp.device.quad.dac.kicad:ESD441DPLR, F.Cu at (90.0, -97.0)
- added TVS5: ESD441DPLR, harp.device.quad.dac.kicad:ESD441DPLR, F.Cu at (6.00, -52.0)
- added TVS6: ESD441DPLR, harp.device.quad.dac.kicad:ESD441DPLR, F.Cu at (248.7, 53.8)
- added TVS7: ESD441DPLR, harp.device.quad.dac.kicad:ESD441DPLR, F.Cu at (248.7, 60.5)
- added TVS8: ESD441DPLR, harp.device.quad.dac.kicad:ESD441DPLR, F.Cu at (248.8, 86.2)
- added TVS9: ESD441DPLR, harp.device.quad.dac.kicad:ESD441DPLR, F.Cu at (248.7, 78.6)
- added U10: LT1678CS8#PBF, harp.device.quad.dac.kicad:SOIC127P599X175-8N, F.Cu at (-346.5, 65.5)
- added U11: LT1678CS8#PBF, harp.device.quad.dac.kicad:SOIC127P599X175-8N, F.Cu at (-347.5, 94.5)
- added U12: LT1678CS8#PBF, harp.device.quad.dac.kicad:SOIC127P599X175-8N, F.Cu at (-347.0, 120.0)
- added U13: LT1678CS8#PBF, harp.device.quad.dac.kicad:SOIC127P599X175-8N, F.Cu at (-339.0, 140.0)
- added U14: LT1461CIS8-2.5#PBF, harp.device.quad.dac.kicad:SOIC127P599X175-8N, F.Cu at (-379.1, 62.0)
- added U15: LT1678CS8#PBF, harp.device.quad.dac.kicad:SOIC127P599X175-8N, F.Cu at (-109.0, 45.0)
- added U16: LT1678CS8#PBF, harp.device.quad.dac.kicad:SOIC127P599X175-8N, F.Cu at (-110.0, 26.0)
- added U17: LM211DRG4, harp.device.quad.dac.kicad:SOIC127P600X175-8N, F.Cu at (-113.0, 79.0)
- added U18: LM211DRG4, harp.device.quad.dac.kicad:SOIC127P600X175-8N, F.Cu at (-114.0, 93.0)
- added U19: LM211DRG4, harp.device.quad.dac.kicad:SOIC127P600X175-8N, F.Cu at (-114.0, 118.0)
- added U20: LM211DRG4, harp.device.quad.dac.kicad:SOIC127P600X175-8N, F.Cu at (-115.0, 152.0)
- added U26: LTC3122HMSE#PBF, harp.device.quad.dac.kicad:SOP65P490X110-13N, F.Cu at (418.0, 249.7)
- added U27: LTC3115IDHD-2#WPBF, harp.device.quad.dac.kicad:SON50P400X500X80-17N-D, F.Cu at (412.0, 165.0)
- added U30: LM2990SX-12, harp.device.quad.dac.kicad:KTT0003B, F.Cu at (405.0, 221.7)
- added U6: LTC2642ACDD-16#PBF, harp.device.quad.dac.kicad:SON50P300X300X80-11N-D, F.Cu at (-340.1, 64.8)
- added U7: LTC2642ACDD-16#PBF, harp.device.quad.dac.kicad:SON50P300X300X80-11N-D, F.Cu at (-341.1, 91.6)
- added U8: LTC2642ACDD-16#PBF, harp.device.quad.dac.kicad:SON50P300X300X80-11N-D, F.Cu at (-340.6, 114.9)
- added U9: LTC2642ACDD-16#PBF, harp.device.quad.dac.kicad:SON50P300X300X80-11N-D, F.Cu at (-346.0, 141.0)
- D1, D2, D3, D4: value BAT43W-V -> BAT43W-7-F
- D7, D8: footprint Diode_SMD:D_MiniMELF -> harp.device.quad.dac.kicad:D_MiniMELF
- FID1, FID2, FID3, FID4: footprint Fiducial:Fiducial_0.5mm_Mask1mm -> harp.device.quad.dac.kicad:Fiducial_0.5mm_Mask1mm
- J2: footprint Connector_PinHeader_2.54mm:PinHeader_1x03_P2.54mm_Vertical -> harp.device.quad.dac.kicad:PinHeader_1x03_P2.54mm_Vertical
- J3: footprint Connector_USB:USB_C_Receptacle_JAE_DX07S016JA1R1500 -> harp.device.quad.dac.kicad:USB_C_Receptacle_JAE_DX07S016JA1R1500
- J4: footprint Connector_Audio:Jack_3.5mm_CUI_SJ-3524-SMT_Horizontal -> harp.device.quad.dac.kicad:Jack_3.5mm_CUI_SJ-3524-SMT_Horizontal
- LED4, LED5, LED6, LED7, LED8, LED9: footprint LED_SMD:LED_0603_1608Metric_Pad1.05x0.95mm_HandSolder -> harp.device.quad.dac.kicad:LED_0603_1608Metric_Pad1.05x0.95mm_HandSolder
- U21: footprint Package_SO:TSSOP-8_3x3mm_P0.65mm -> harp.device.quad.dac.kicad:SOP50P310X90-8N
- U22: footprint Package_SO:SOIC-16W_7.5x10.3mm_P1.27mm -> harp.device.quad.dac.kicad:SOIC-16W_7.5x10.3mm_P1.27mm
- U23, U24, U25, U31, U32: footprint Package_SO:VSSOP-8_2.3x2mm_P0.5mm -> harp.device.quad.dac.kicad:VSSOP-8_2.3x2mm_P0.5mm
- U28, U29: footprint Package_TO_SOT_SMD:SOT-223-3_TabPin2 -> harp.device.quad.dac.kicad:SOT-223-3_TabPin2
- moved R1 541.2 mm to (-352.0, -198.0)
- moved C12 535.5 mm to (-348.0, -198.0)
- moved R2 534.9 mm to (-347.0, -192.0)
- moved R6 534.7 mm to (-350.0, -178.0)
- moved R4 534.5 mm to (-356.0, -170.0), turned to 90 degrees
- moved C36 534.1 mm to (-384.0, 88.0)
- moved R5 532.7 mm to (-357.0, -162.0), turned to 90 degrees
- moved C30 529.6 mm to (-384.2, 81.7)
- moved C31 529.6 mm to (-384.2, 83.7)
- moved R3 529.3 mm to (-346.0, -180.0)
- moved U2 528.5 mm to (-318.0, -204.0)
- moved C13 527.8 mm to (-346.1, -182.8)
- moved R10 527.5 mm to (-327.0, -203.0)
- moved R11 527.5 mm to (-327.0, -201.0)
- moved R7 526.0 mm to (-347.0, -169.0)
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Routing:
- net VBUS: track 0.00 -> 16.4 mm
- net +3.3V: track 0.00 -> 3.12 mm
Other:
- board outline added: 80 x 59.5 mm
- copper layers 2 -> 4

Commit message: Some improvements have been made to the layout.
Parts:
- added TVS16: ESDSB12VLB-TP, harp.device.quad.dac.kicad:ESDSB12VLBTP, F.Cu at (197.3, 50.1)
- added TVS17: ESDSB12VLB-TP, harp.device.quad.dac.kicad:ESDSB12VLBTP, F.Cu at (210.0, 50.1)
- added TVS18: ESDSB12VLB-TP, harp.device.quad.dac.kicad:ESDSB12VLBTP, F.Cu at (235.4, 50.1)
- added TVS19: ESDSB12VLB-TP, harp.device.quad.dac.kicad:ESDSB12VLBTP, F.Cu at (222.7, 50.1)
- C30, C31, C36, C37, C38, C43, C48, C49, C60, C61, C62, C63, C64, C65, C66, C67, C68, C69, C70, C71, C72, C73, C74, C75, C76, C77, C78, C79, C80, C81, C82, C83, C84, C85, C86, C87, C88, C89, C90, C91, D1, D2, D3, D4, Jump2, Jump3, R22, R39, R40, R41, R42, R43, R44, R45, R46, R47, R48, R49, R50, R51, R52, R53, R54, R55, R56, R57, R58, R59, R60, R61, R62, R63, R64, R65, R66, R67, R68, R69, R70, R71, R72, R73, R74, R75, R76, R77, R78, R79, R80, R81, R82, U14, U15, U16, U17, U18, U19, U20: moved to B.Cu
- moved R22 605.4 mm to (219.8, 70.0), turned to -90 degrees
- moved U14 598.2 mm to (218.9, 75.1), turned to -90 degrees
- moved C37 595.2 mm to (218.3, 70.1), turned to -90 degrees
- moved C43 594.5 mm to (220.3, 82.4)
- moved C48 591.7 mm to (220.3, 80.9)
- moved C49 591.6 mm to (220.3, 79.4), turned to 180 degrees
- moved R24 591.2 mm to (242.9, 57.1), turned to 90 degrees
- moved C38 590.9 mm to (216.8, 70.1), turned to 90 degrees
- moved C30 590.3 mm to (206.1, 73.6), turned to -90 degrees
- moved Jump3 589.7 mm to (211.5, 73.7), turned to 90 degrees
- moved C31 588.8 mm to (204.6, 73.6), turned to 90 degrees
- moved C36 587.2 mm to (203.0, 73.6), turned to 90 degrees
- moved J20 587.2 mm to (209.3, 74.8), turned to 180 degrees
- moved R31 586.4 mm to (240.8, 53.9), turned to 90 degrees
- moved J21 586.2 mm to (213.0, 72.3)
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- renumbered RShunt1 to RSh1, RShunt2 to RSh2, RShunt3 to RSh3, RShunt4 to RSh4
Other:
- board size 80 x 59.5 mm -> 118.1 x 59.5 mm
